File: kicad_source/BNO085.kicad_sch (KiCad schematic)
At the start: 16 parts, among them U16 BNO085, Y2 DNI

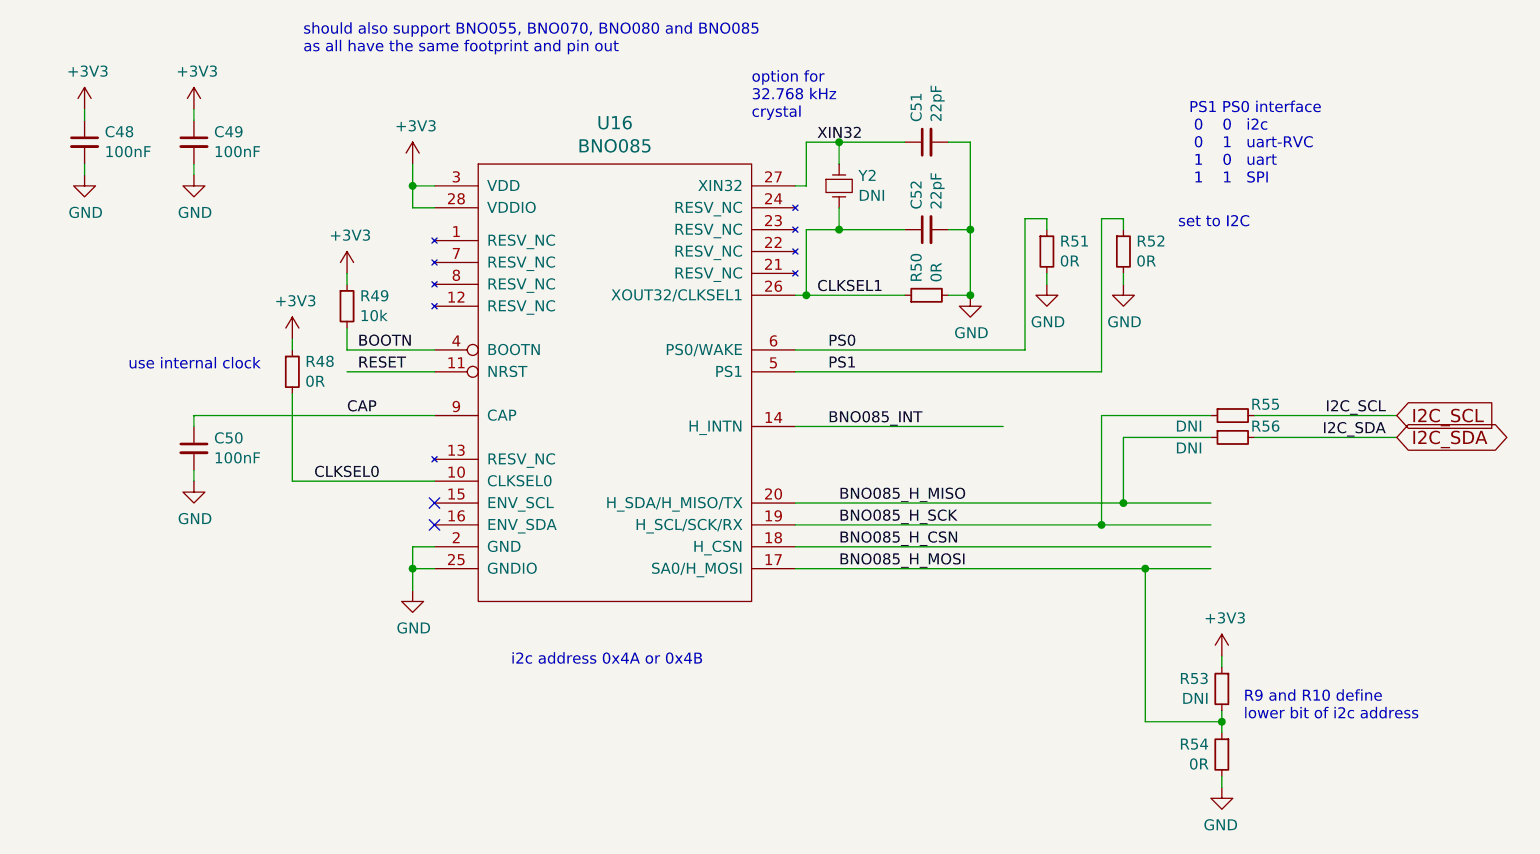
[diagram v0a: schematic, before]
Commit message: added GNSS u-blox max-m10
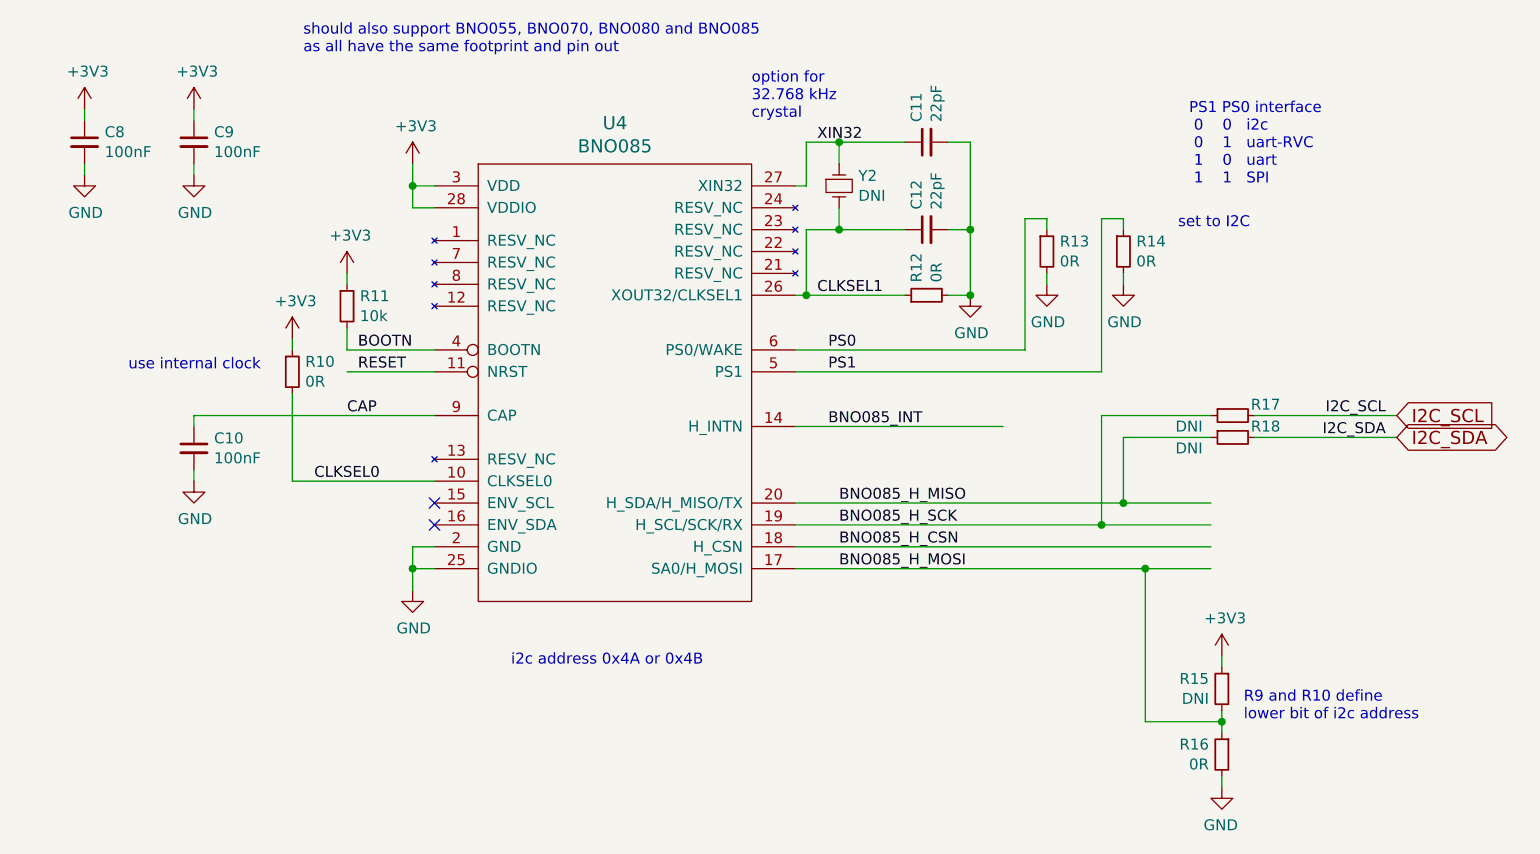
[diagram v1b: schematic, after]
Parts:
- renumbered C50 to C10, C51 to C11, C52 to C12, C48 to C8, C49 to C9, R48 to R10, R49 to R11, R50 to R12, R51 to R13, R52 to R14, R53 to R15, R54 to R16, R55 to R17, R56 to R18, U16 to U4
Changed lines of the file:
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@@
 		(on_board yes)
 		(dnp no)
-		(property "Reference" "U16"
+		(property "Reference" "U4"
 			(at 84.455 25.7302 0)
 			(effects
@@
 			(project "CyphalGNSSIMUBase-CAN"
 				(path "/9d6d512e-1439-4aa2-b0d9-afb2dddd9146/c16f48f1-b203-4e3b-a63b-33c1b1e484ca"
-					(reference "U16")
+					(reference "U4")
 					(unit 1)
 				)
@@
 		(on_board yes)
 		(dnp no)
-		(property "Reference" "#PWR0142"
+		(property "Reference" "#PWR46"
 			(at 60.96 86.36 0)
 			(effects
@@
 			(project "CyphalGNSSIMUBase-CAN"
 				(path "/9d6d512e-1439-4aa2-b0d9-afb2dddd9146/c16f48f1-b203-4e3b-a63b-33c1b1e484ca"
-					(reference "#PWR0142")
+					(reference "#PWR46")
 					(unit 1)
 				)
@@
 		(on_board yes)
 		(dnp no)
-		(property "Reference" "R51"
+		(property "Reference" "R13"
 			(at 136.1186 39.4716 0)
 			(effects
@@
 			(project "CyphalGNSSIMUBase-CAN"
 				(path "/9d6d512e-1439-4aa2-b0d9-afb2dddd9146/c16f48f1-b203-4e3b-a63b-33c1b1e484ca"
-					(reference "R51")
+					(reference "R13")
 					(unit 1)
 				)
@@
 		(on_board yes)
 		(dnp no)
-		(property "Reference" "#PWR0144"
+		(property "Reference" "#PWR48"
 			(at 134.62 50.8 0)
 			(effects
@@
 			(project "CyphalGNSSIMUBase-CAN"
 				(path "/9d6d512e-1439-4aa2-b0d9-afb2dddd9146/c16f48f1-b203-4e3b-a63b-33c1b1e484ca"
-					(reference "#PWR0144")
+					(reference "#PWR48")
 					(unit 1)
 				)
@@
 		(on_board yes)
 		(dnp no)
-		(property "Reference" "R52"
+		(property "Reference" "R14"
 			(at 145.0086 39.4716 0)
 			(effects
@@
 			(project "CyphalGNSSIMUBase-CAN"
 				(path "/9d6d512e-1439-4aa2-b0d9-afb2dddd9146/c16f48f1-b203-4e3b-a63b-33c1b1e484ca"
-					(reference "R52")
+					(reference "R14")
 					(unit 1)
 				)
@@
 		(on_board yes)
 		(dnp no)
-		(property "Reference" "#PWR0145"
+		(property "Reference" "#PWR49"
 			(at 143.51 50.8 0)
 			(effects
@@
 			(project "CyphalGNSSIMUBase-CAN"
 				(path "/9d6d512e-1439-4aa2-b0d9-afb2dddd9146/c16f48f1-b203-4e3b-a63b-33c1b1e484ca"
-					(reference "#PWR0145")
+					(reference "#PWR49")
 					(unit 1)
 				)
@@
 		(on_board yes)
 		(dnp no)
-		(property "Reference" "C50"
+		(property "Reference" "C10"
 			(at 37.8968 62.3316 0)
 			(effects
@@
 			(project "CyphalGNSSIMUBase-CAN"
 				(path "/9d6d512e-1439-4aa2-b0d9-afb2dddd9146/c16f48f1-b203-4e3b-a63b-33c1b1e484ca"
-					(reference "C50")
+					(reference "C10")
 					(unit 1)
 				)
@@
 		(on_board yes)
 		(dnp no)
-		(property "Reference" "#PWR0138"
+		(property "Reference" "#PWR42"
 			(at 35.56 73.66 0)
 			(effects
@@
 			(project "CyphalGNSSIMUBase-CAN"
 				(path "/9d6d512e-1439-4aa2-b0d9-afb2dddd9146/c16f48f1-b203-4e3b-a63b-33c1b1e484ca"
-					(reference "#PWR0138")
+					(reference "#PWR42")
 					(unit 1)
 				)
@@
 		(on_board yes)
 		(dnp no)
-		(property "Reference" "R54"
+		(property "Reference" "R16"
 			(at 153.4414 97.8916 0)
 			(effects
@@
 			(project "CyphalGNSSIMUBase-CAN"
 				(path "/9d6d512e-1439-4aa2-b0d9-afb2dddd9146/c16f48f1-b203-4e3b-a63b-33c1b1e484ca"
-					(reference "R54")
+					(reference "R16")
 					(unit 1)
 				)
@@
 		(on_board yes)
 		(dnp no)
-		(property "Reference" "R53"
+		(property "Reference" "R15"
 			(at 153.4414 90.2716 0)
 			(effects
@@
 			(project "CyphalGNSSIMUBase-CAN"
 				(path "/9d6d512e-1439-4aa2-b0d9-afb2dddd9146/c16f48f1-b203-4e3b-a63b-33c1b1e484ca"
-					(reference "R53")
+					(reference "R15")
 					(unit 1)
 				)
@@
 		(on_board yes)
 		(dnp no)
-		(property "Reference" "#PWR0147"
+		(property "Reference" "#PWR51"
 			(at 154.94 109.22 0)
 			(effects
@@
 			(project "CyphalGNSSIMUBase-CAN"
 				(path "/9d6d512e-1439-4aa2-b0d9-afb2dddd9146/c16f48f1-b203-4e3b-a63b-33c1b1e484ca"
-					(reference "#PWR0147")
+					(reference "#PWR51")
 					(unit 1)
 				)
@@
 		(on_board yes)
 		(dnp no)
-		(property "Reference" "R56"
+		(property "Reference" "R18"
 			(at 160.02 60.96 90)
 			(effects
@@
 			(project "CyphalGNSSIMUBase-CAN"
 				(path "/9d6d512e-1439-4aa2-b0d9-afb2dddd9146/c16f48f1-b203-4e3b-a63b-33c1b1e484ca"
-					(reference "R56")
+					(reference "R18")
 					(unit 1)
 				)
@@
 		(on_board yes)
 		(dnp no)
-		(property "Reference" "R55"
+		(property "Reference" "R17"
 			(at 160.02 58.42 90)
 			(effects
@@
 			(project "CyphalGNSSIMUBase-CAN"
 				(path "/9d6d512e-1439-4aa2-b0d9-afb2dddd9146/c16f48f1-b203-4e3b-a63b-33c1b1e484ca"
-					(reference "R55")
+					(reference "R17")
 					(unit 1)
 				)
@@
 		(on_board yes)
 		(dnp no)
-		(property "Reference" "#PWR0143"
+		(property "Reference" "#PWR47"
 			(at 125.73 52.07 0)
 			(effects
@@
 			(project "CyphalGNSSIMUBase-CAN"
 				(path "/9d6d512e-1439-4aa2-b0d9-afb2dddd9146/c16f48f1-b203-4e3b-a63b-33c1b1e484ca"
-					(reference "#PWR0143")
+					(reference "#PWR47")
 					(unit 1)
 				)
@@
 		(on_board yes)
 		(dnp no)
-		(property "Reference" "R50"
+		(property "Reference" "R12"
 			(at 119.4816 44.2214 0)
 			(effects
@@
 			(project "CyphalGNSSIMUBase-CAN"
 				(path "/9d6d512e-1439-4aa2-b0d9-afb2dddd9146/c16f48f1-b203-4e3b-a63b-33c1b1e484ca"
-					(reference "R50")
+					(reference "R12")
 					(unit 1)
 				)
@@
 		(on_board yes)
 		(dnp no)
-		(property "Reference" "R48"
+		(property "Reference" "R10"
 			(at 48.4886 53.4416 0)
 			(effects
@@
 			(project "CyphalGNSSIMUBase-CAN"
 				(path "/9d6d512e-1439-4aa2-b0d9-afb2dddd9146/c16f48f1-b203-4e3b-a63b-33c1b1e484ca"
-					(reference "R48")
+					(reference "R10")
 					(unit 1)
 				)
@@
 		(on_board yes)
 		(dnp no)
-		(property "Reference" "C48"
+		(property "Reference" "C8"
 			(at 25.1968 26.7716 0)
 			(effects
@@
 			(project "CyphalGNSSIMUBase-CAN"
 				(path "/9d6d512e-1439-4aa2-b0d9-afb2dddd9146/c16f48f1-b203-4e3b-a63b-33c1b1e484ca"
-					(reference "C48")
+					(reference "C8")
 					(unit 1)
 				)
@@
 		(on_board yes)
 		(dnp no)
-		(property "Reference" "#PWR0135"
+		(property "Reference" "#PWR39"
 			(at 22.86 38.1 0)
 			(effects
@@
 			(project "CyphalGNSSIMUBase-CAN"
 				(path "/9d6d512e-1439-4aa2-b0d9-afb2dddd9146/c16f48f1-b203-4e3b-a63b-33c1b1e484ca"
-					(reference "#PWR0135")
+					(reference "#PWR39")
 					(unit 1)
 				)
@@
 		(on_board yes)
 		(dnp no)
-		(property "Reference" "C49"
+		(property "Reference" "C9"
 			(at 37.8968 26.7716 0)
 			(effects
@@
 			(project "CyphalGNSSIMUBase-CAN"
 				(path "/9d6d512e-1439-4aa2-b0d9-afb2dddd9146/c16f48f1-b203-4e3b-a63b-33c1b1e484ca"
-					(reference "C49")
+					(reference "C9")
 					(unit 1)
 				)
@@
 		(on_board yes)
 		(dnp no)
-		(property "Reference" "#PWR0137"
+		(property "Reference" "#PWR41"
 			(at 35.56 38.1 0)
 			(effects
@@
 			(project "CyphalGNSSIMUBase-CAN"
 				(path "/9d6d512e-1439-4aa2-b0d9-afb2dddd9146/c16f48f1-b203-4e3b-a63b-33c1b1e484ca"
-					(reference "#PWR0137")
+					(reference "#PWR41")
 					(unit 1)
 				)
@@
 		(on_board yes)
 		(dnp no)
-		(property "Reference" "R49"
+		(property "Reference" "R11"
 			(at 54.8386 45.8216 0)
 			(effects
@@
 			(project "CyphalGNSSIMUBase-CAN"
 				(path "/9d6d512e-1439-4aa2-b0d9-afb2dddd9146/c16f48f1-b203-4e3b-a63b-33c1b1e484ca"
-					(reference "R49")
+					(reference "R11")
 					(unit 1)
 				)
@@
 		(on_board yes)
 		(dnp no)
-		(property "Reference" "C52"
+		(property "Reference" "C12"
 			(at 119.4816 35.7632 0)
 			(effects
@@
 			(project "CyphalGNSSIMUBase-CAN"
 				(path "/9d6d512e-1439-4aa2-b0d9-afb2dddd9146/c16f48f1-b203-4e3b-a63b-33c1b1e484ca"
-					(reference "C52")
+					(reference "C12")
 					(unit 1)
 				)
@@
 		(on_board yes)
 		(dnp no)
-		(property "Reference" "C51"
+		(property "Reference" "C11"
 			(at 119.4816 25.6032 0)
 			(effects
@@
 			(project "CyphalGNSSIMUBase-CAN"
 				(path "/9d6d512e-1439-4aa2-b0d9-afb2dddd9146/c16f48f1-b203-4e3b-a63b-33c1b1e484ca"
-					(reference "C51")
+					(reference "C11")
 					(unit 1)
 				)
@@
 		(on_board yes)
 		(dnp no)
-		(property "Reference" "#PWR4"
+		(property "Reference" "#PWR40"
 			(at 35.56 27.94 0)
 			(effects
@@
 			(project "CyphalGNSSIMUBase-CAN"
 				(path "/9d6d512e-1439-4aa2-b0d9-afb2dddd9146/c16f48f1-b203-4e3b-a63b-33c1b1e484ca"
-					(reference "#PWR4")
+					(reference "#PWR40")
 					(unit 1)
 				)
@@
 		(on_board yes)
 		(dnp no)
-		(property "Reference" "#PWR10"
+		(property "Reference" "#PWR50"
 			(at 154.94 91.44 0)
 			(effects
@@
 			(project "CyphalGNSSIMUBase-CAN"
 				(path "/9d6d512e-1439-4aa2-b0d9-afb2dddd9146/c16f48f1-b203-4e3b-a63b-33c1b1e484ca"
-					(reference "#PWR10")
+					(reference "#PWR50")
 					(unit 1)
 				)
@@
 		(on_board yes)
 		(dnp no)
-		(property "Reference" "#PWR3"
+		(property "Reference" "#PWR38"
 			(at 22.86 27.94 0)
 			(effects
@@
 			(project "CyphalGNSSIMUBase-CAN"
 				(path "/9d6d512e-1439-4aa2-b0d9-afb2dddd9146/c16f48f1-b203-4e3b-a63b-33c1b1e484ca"
-					(reference "#PWR3")
+					(reference "#PWR38")
 					(unit 1)
 				)
@@
 		(on_board yes)
 		(dnp no)
-		(property "Reference" "#PWR6"
+		(property "Reference" "#PWR45"
 			(at 60.96 34.29 0)
 			(effects
@@
 			(project "CyphalGNSSIMUBase-CAN"
 				(path "/9d6d512e-1439-4aa2-b0d9-afb2dddd9146/c16f48f1-b203-4e3b-a63b-33c1b1e484ca"
-					(reference "#PWR6")
+					(reference "#PWR45")
 					(unit 1)
 				)
@@
 		(on_board yes)
 		(dnp no)
-		(property "Reference" "#PWR7"
+		(property "Reference" "#PWR44"
 			(at 53.34 46.99 0)
 			(effects
@@
 			(project "CyphalGNSSIMUBase-CAN"
 				(path "/9d6d512e-1439-4aa2-b0d9-afb2dddd9146/c16f48f1-b203-4e3b-a63b-33c1b1e484ca"
-					(reference "#PWR7")
+					(reference "#PWR44")
 					(unit 1)
 				)
@@
 		(on_board yes)
 		(dnp no)
-		(property "Reference" "#PWR9"
+		(property "Reference" "#PWR43"
 			(at 46.99 54.61 0)
 			(effects
@@
 			(project "CyphalGNSSIMUBase-CAN"
 				(path "/9d6d512e-1439-4aa2-b0d9-afb2dddd9146/c16f48f1-b203-4e3b-a63b-33c1b1e484ca"
-					(reference "#PWR9")
-					(unit 1)
-				)
+					(reference "#PWR43")
+					(unit 1)
+				)
